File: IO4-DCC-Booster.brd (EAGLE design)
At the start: 100 x 100 mm, 52 parts, among them CON6 I2C, J2 NCE, J3 NCE, J4 LNET, J6 TRACK, J7 IBT-2, J8 CTL-IBT-2, Q6 2N7002

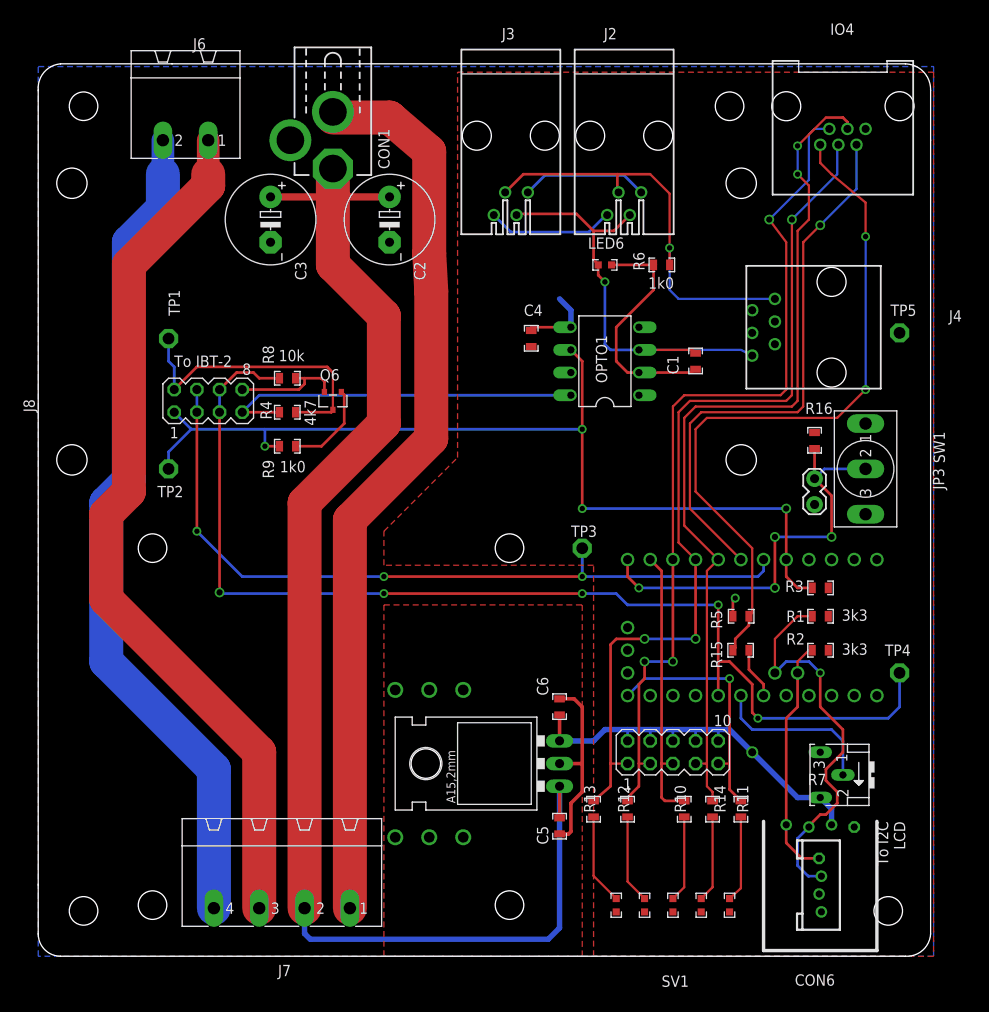
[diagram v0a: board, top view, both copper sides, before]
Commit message: Rework, DC supply, simpler trace layout
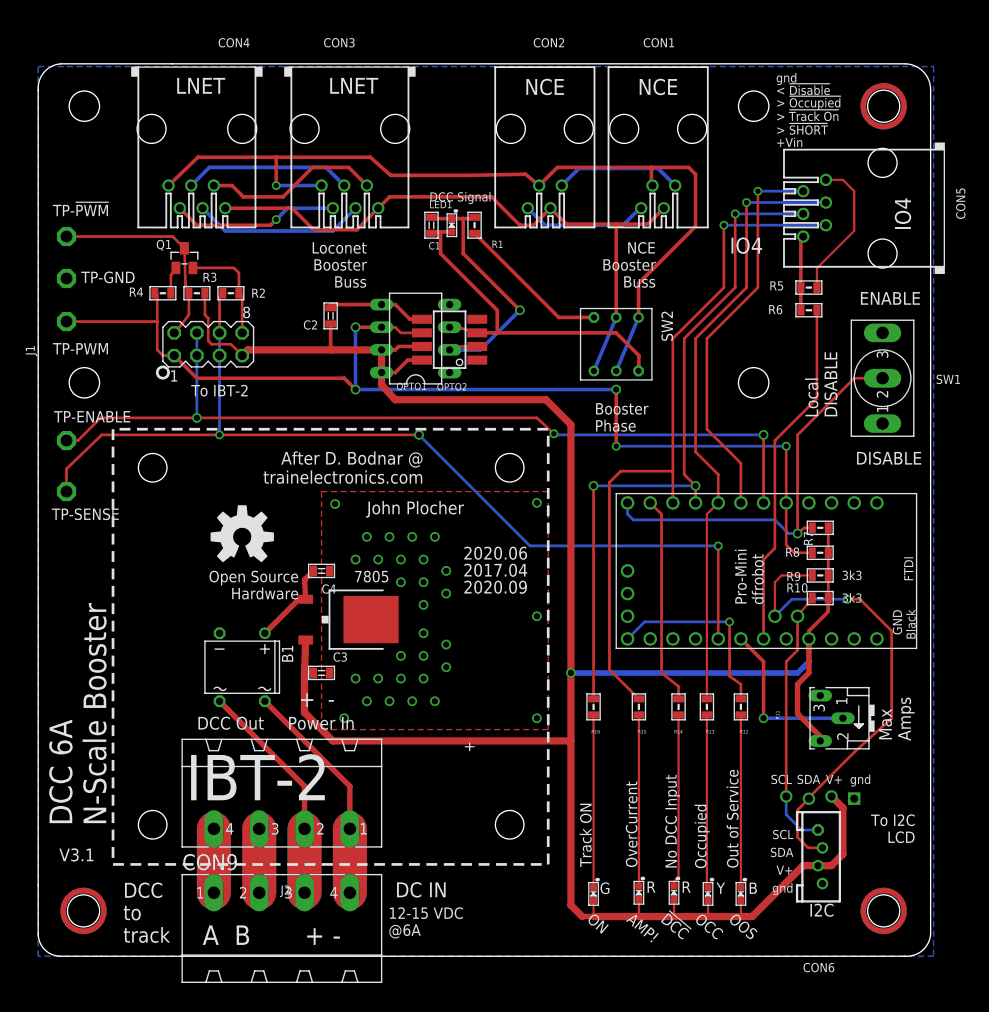
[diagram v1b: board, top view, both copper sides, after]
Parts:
- removed C5, C6: 0.1uF, SPCoast:0805-CAP
- removed IO4: IO-4, SPCoast:RJ25-INVERTED
- removed J3: NCE, con-amp:555980-1
- removed J4: LNET, SPCoast:RJ25-TOP
- removed J6: TRACK, con-phoenix-508:MSTBA2
- removed J7: IBT-2, con-phoenix-508:MSTBA4
- removed J8: CTL-IBT-2, con-lstb:MA04-2
- removed JP3: (no value), SPCoast:1X02_LOCK
- removed Q6: 2N7002, microbuilder:SOT23-R
- removed SV1: (no value), con-lstb:MA05-2
- removed TP1, TP2, TP3, TP4, TP5: TPPAD1-13, testpad:P1-13
- added B1: DBDB101G, SPCoast:DB
- added CON2: NCE, SPCoast:555980-1
- added CON3, CON4: LNET, SPCoast:RJ25-PANEL
- added CON5: IO4, SPCoast:RJ25-PANEL
- added CON9: (no value), SPCoast:MSTBA4
- added J1: CTL-IBT-2, con-lstb:MA04-2
- added OPTO2: 6N137, SPCoast:SM8
- added Q1: 2N7002, SPCoast:SOT23
- added SW2: (no value), SPCoast:8X8-SQ-PB
- added TP-!PWM, TP-ENABLE, TP-GND, TP-PWM, TP-SENSE: TPPAD1-13, testpad:P1-13
- added U$2: IBT-2, SPCoast:IBT-2
- added U$3, U$4, U$5: MOUNTINGHOLE, SPCoast:MOUNTINGHOLE
- BOARD1: value (none) -> BOARD100X100-NOHOLES
- C2: value 1000uF -> 0.1uF; device SPCoast:E5-10,5 -> SPCoast:0805-CAP
- C3: value 1000uF -> 10uF; device SPCoast:E5-10,5 -> SPCoast:0805-CAP
- CON1: value (none) -> NCE; device SPCoast:DCJ0202 -> SPCoast:555980-1
- J2: value NCE -> IBT-2; device con-amp:555980-1 -> con-phoenix-508:MSTBA4
- LED1, LED3: value R -> Y
- LED4: value G -> R
- LED5: value Y -> R
- LED6: value DCC -> G
- LOGO1: value DOC-OSHW-LOGOL -> DOC-OSHW-LOGO-L
- R1: value 3k3 -> 1k0
- R10: value 2k2 -> 3k3
- R11: value 2k2 -> 10k; device SPCoast:0805-RES -> SPCoast:B25X
- R15: value 1k0 -> 2k2
- R16: value 4k7 -> 2k2
- R2: value 3k3 -> 10k
- R4: value 4k7 -> 1k0
- R5, R6: value 1k0 -> 10k
- R7: value 10k -> 4k7; device SPCoast:B25X -> SPCoast:0805-RES
- R8: value 10k -> 4k7
- R9: value 1k0 -> 3k3
- VR1: device SPCoast:78XXL -> SPCoast:TO-252
- moved J2 82.1 mm to (27.3, 19.4)
- moved LED1 80.1 mm to (46.4, 81.9), turned to 270 degrees
- moved R3 77.3 mm to (17.8, 74.3)
- moved R2 77.2 mm to (21.6, 74.3), turned to 180 degrees
- moved LED6 70.5 mm to (62.2, 6.99)
- moved R8 62.8 mm to (87.6, 45.2), turned to 0 degrees
- moved R9 61.4 mm to (87.6, 42.7), turned to 0 degrees
- moved R1 58.5 mm to (48.9, 81.9), turned to 270 degrees
- moved C3 51.1 mm to (31.8, 31.8), turned to 0 degrees
- moved R16 38.8 mm to (62.2, 27.9), turned to 270 degrees
- moved R5 37.6 mm to (86.4, 74.9), turned to 180 degrees
- moved CON1 36.5 mm to (69.5, 92.7)
- moved C4 35.1 mm to (31.8, 43.2), turned to 0 degrees
- moved C1 33.3 mm to (44.1, 81.9), turned to 270 degrees
- moved R10 28.1 mm to (87.6, 40.1), turned to 0 degrees
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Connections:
- removed net DCC+: J6.1, J7.3
- removed net DCC-: J6.2, J7.4
- removed net N$2: C1.1, LED6.C, OPTO1.2, R6.1
- removed net N$4: ARDUINO1.AD1, R7.3
- new net DCC-A-OUT: C1.2, LED1.A, OPTO1.3, OPTO2.3, SW2.1C
- new net DCC-B-LIMITED: C1.1, LED1.C, OPTO1.2, OPTO2.2, R1.1
- new net DCC-B-OUT: R1.2, SW2.2C
- new net LIMIT: ARDUINO1.AD1, R11.3
- new net N$11: CON3.3, CON4.3
- new net N$16: CON3.2, CON4.2
- new net N$19: B1.+, C4.1, VR1.1
- new net N$8: CON3.5, CON4.5
- new net N$9: CON3.4, CON4.4
- new net TRACK-A: CON9.1, J2.4
- new net TRACK-B: CON9.2, J2.3
- new net V15-: B1.AC2, CON9.4, J2.1
- net !IOCCUPIED: now also CON5.4, R13.1; no longer IO4.4, R14.1, SV1.7
- net !ISHORT: now also CON5.2, R15.1; no longer IO4.2, R12.1, SV1.3
- net !ITRACK_ON: now also CON5.3, R16.1; no longer IO4.3, R13.1, SV1.1
- net !KPOFF: now also CON5.5; no longer IO4.5
- net !LOCAL_DISABLE: now also R7.1; no longer JP3.1, R16.1
- net !NO_SIGNAL: now also R14.1; no longer R10.1, SV1.5
- net !OUT_OF_SERVICE: now also R12.1; no longer R11.1, SV1.9
- net !PWM: now also J1.2, Q1.3, R3.1, TP-!PWM.TP; no longer J8.2, Q6.3, R4.1, TP1.TP
- net DCC-A: now also CON1.2, CON2.2, CON3.1, CON4.1, SW2.1A, SW2.2B; no longer C1.2, J2.2, J3.2, J4.1, LED6.A, OPTO1.3
- net DCC-B: now also CON1.3, CON2.3, CON3.6, CON4.6, SW2.1B, SW2.2A; no longer J2.3, J3.3, J4.6, R6.2
- net ENABLE: now also J1.3, J1.4, TP-ENABLE.TP; no longer J8.3, J8.4, TP3.TP
- net GND: now also B1.-, C2.2, C3.2, CON5.6, J1.8, OPTO2.5, Q1.2, R11.1, R2.1, TP-GND.TP, VR1.2; no longer C2.-, C3.-, C5.2, C6.2, CON1.2, CON1.3, IO4.6, J7.1, J8.8, JP3.2, Q6.2, R7.1, R8.1, TP5.TP, VR1.GND
- net N$1: now also Q1.1, R4.1; no longer Q6.1, R9.1
- net N$10: now also LED4.C, R14.2; no longer LED1.C, R10.2
- net N$12: now also R12.2; no longer R11.2
- net N$13: now also LED3.C, R13.2; no longer LED5.C, R14.2
- net N$14: now also LED6.C, R16.2; no longer LED4.C, R13.2
- net N$15: now also LED5.C, R15.2; no longer LED3.C, R12.2
- net N$6: now also CON1.4, CON2.4; no longer J2.4, J3.4
- net N$7: now also CON1.1, CON2.1; no longer J2.1, J3.1
- net PWM: now also J1.1, OPTO2.6, R4.2, R8.1, TP-PWM.TP; no longer J8.1, R3.1, R9.2, TP2.TP
- net SCL: now also R10.1; no longer R2.1
- net SDA: now also R9.1; no longer R1.1
- net SENSE: now also J1.5, J1.6, R2.2, TP-SENSE.TP; no longer J8.5, J8.6, R8.2, TP4.TP
- net V15+: now also B1.AC1, CON9.3, J2.2; no longer C2.+, C3.+, C5.1, CON1.1, J7.2, VR1.IN
- net VCC: now also C2.1, C3.1, J1.7, LED6.A, OPTO2.7, OPTO2.8, R10.2, R11.2, R8.2, R9.2, VR1.3; no longer C4.1, C6.1, J8.7, LED1.A, R1.2, R16.2, R2.2, R4.2, SV1.10, SV1.2, SV1.4, SV1.6, SV1.8, VR1.OUT
- net VCOMPUTER: now also CON5.1, R6.2; no longer IO4.1, R15.2
- net VCON: now also R6.1; no longer R15.1
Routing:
- net VCC: track 87.5 -> 266.3 mm
- net V15+: track 153.9 -> 32.6 mm
- net GND: track 145.2 -> 39.8 mm, vias 7 -> 31
- net DCC+: track 97.9 -> 0.00 mm
- net DCC-: track 93.7 -> 0.00 mm
- net VCOMPUTER: track 78.9 -> 8.36 mm, vias 2 -> 0
- net DCC-B: track 47.2 -> 98.3 mm
- net DCC-A-OUT: track 0.00 -> 40.4 mm
- net VCON: track 5.76 -> 39.3 mm
- net V15-: track 0.00 -> 32.6 mm
- net DCC-B-LIMITED: track 0.00 -> 30.8 mm, vias 0 -> 1
- net !IOCCUPIED: track 97.5 -> 68.5 mm, vias 2 -> 1
- net N$2: track 27.0 -> 0.00 mm
- net !ITRACK_ON: track 100.0 -> 78.2 mm
- net DCC-A: track 50.9 -> 72.2 mm, vias 1 -> 0
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- removed copper zone on layer 1, net VCC
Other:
- board text added: "!DCC"
- board text added: "- +"
- board text added: "12-15 VDC @6A"
- board text added: "2020.06"
- board text added: "2020.09"
- board text added: "< !Disable"
- board text added: "> !Occupied"
- board text added: "> !SHORT"
- board text added: "> !Track On"
- board text added: "A B"
- board text added: "AMP!"
- board text added: "After D. Bodnar @ trainelectronics.com"
- board text added: "Booster Phase"
- board text added: "DC IN"
- board text added: "DC PWR"
- board text added: "DCC 6A N-Scale Booster"
- board text added: "DCC Signal"
- board text added: "DISABLE"
- board text added: "Local DISABLE"
- board text added: "Loconet Booster Buss"
- board text added: "NCE Booster Buss"
- board text added: "OCC"
- board text added: "OOS"
- board text added: "Track ON"
- board text added: "V3.1"
- board text removed: "!PWM"
- board text removed: "!SHORT >"
- board text removed: "!Track On >"
- board text removed: "!disable <"
- board text removed: "!occupied >"
- board text removed: "(Via d. bodnar @ trainelectronics.com)"
- board text removed: "16VDC"
- board text removed: "5A"
- board text removed: "AC"
- board text removed: "Booster Buss"
- board text removed: "From Transformer"
- board text removed: "LED"
- board text removed: "OFF"
- board text removed: "PWM"
- board text removed: "SENSE"
- board text removed: "TRK PWR"
- board text removed: "Track Power"
- board text removed: "V3.0"

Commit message: normalized values
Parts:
- CON5: value IO4 -> RJ12/6
- CON9: value (none) -> 0.200
- J1: value CTL-IBT-2 -> 2x4-0.100
- LCD: value (none) -> LCD
- SW1: value (none) -> SPDT
- SW2: value (none) -> DPDT
- renumbered U$1 to LCD
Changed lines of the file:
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@@
 <setting verticaltext="up"/>
 </settings>
-<grid distance="50" unitdist="mil" unit="mil" style="dots" multiple="2" display="yes" altdistance="5" altunitdist="mil" altunit="mil"/>
+<grid distance="50" unitdist="mil" unit="mil" style="dots" multiple="2" display="yes" altdistance="25" altunitdist="mil" altunit="mil"/>
 <layers>
 <layer number="1" name="Top" color="4" fill="1" visible="yes" active="yes"/>
@@
 <attribute name="VALUE" x="42.799" y="77.724" size="1.016" layer="27" ratio="10"/>
 </element>
-<element name="CON5" library="SPCoast" package="RJ25-PANEL" value="IO4" x="94.615" y="83.82" smashed="yes" rot="R90">
+<element name="CON5" library="SPCoast" package="RJ25-PANEL" value="RJ12/6" x="94.615" y="83.82" smashed="yes" rot="R90">
 <attribute name="NAME" x="103.886" y="82.55" size="1.016" layer="25" rot="R90"/>
 <attribute name="VALUE" x="99.06" y="87.122" size="1.016" layer="27" rot="R90"/>
 </element>
-<element name="J1" library="con-lstb" package="MA04-2" value="CTL-IBT-2" x="19.05" y="68.58" smashed="yes">
+<element name="J1" library="con-lstb" package="MA04-2" value="2x4-0.100" x="19.05" y="68.58" smashed="yes">
 <attribute name="MF" value="" x="19.05" y="68.58" size="1.778" layer="27" display="off"/>
 <attribute name="MPN" value="" x="19.05" y="68.58" size="1.778" layer="27" display="off"/>
@@
 <attribute name="VALUE" x="14.478" y="73.025" size="1.016" layer="27" ratio="10" rot="R180"/>
 </element>
-<element name="U$1" library="SPCoast" package="LCD-16X2-SILK" value="" x="42.672" y="79.756" smashed="yes"/>
+<element name="LCD" library="SPCoast" package="LCD-16X2-SILK" value="LCD" x="42.672" y="79.756" smashed="yes"/>
 <element name="LED4" library="SPCoast" package="0603-LED" value="R" x="71.247" y="7.112" smashed="yes" rot="R270">
 <attribute name="VALUE" x="73.152" y="8.382" size="1.27" layer="21" rot="R180"/>
@@
 <attribute name="VALUE" x="90.043" y="47.371" size="1.016" layer="27"/>
 </element>
-<element name="SW1" library="SPCoast" package="SWITCH-SPDT-508" value="" x="94.615" y="64.77" smashed="yes" rot="R90">
+<element name="SW1" library="SPCoast" package="SWITCH-SPDT-508" value="SPDT" x="94.615" y="64.77" smashed="yes" rot="R90">
 <attribute name="NAME" x="100.584" y="64.135" size="1.016" layer="25"/>
 <attribute name="VALUE" x="100.33" y="58.42" size="1.778" layer="27" ratio="10" rot="R90"/>
@@
 <element name="U$4" library="SPCoast" package="MOUNTINGHOLE" value="MOUNTINGHOLE" x="94.742" y="5.08"/>
 <element name="U$5" library="SPCoast" package="MOUNTINGHOLE" value="MOUNTINGHOLE" x="94.742" y="95.25"/>
-<element name="SW2" library="SPCoast" package="8X8-SQ-PB" value="" x="64.77" y="68.58" rot="R270"/>
-<element name="CON9" library="SPCoast" package="MSTBA4" value="" x="27.305" y="2.032"/>
+<element name="SW2" library="SPCoast" package="8X8-SQ-PB" value="DPDT" x="64.77" y="68.58" rot="R270"/>
+<element name="CON9" library="SPCoast" package="MSTBA4" value="0.200" x="27.305" y="2.032"/>
 </elements>
 <signals>
